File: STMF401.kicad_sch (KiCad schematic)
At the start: 26 parts, among them J6 Conn_01x04_Pin, U3 STM32F407VETx, Y1 X322525MQB4SI, Y2 SMD03215C2

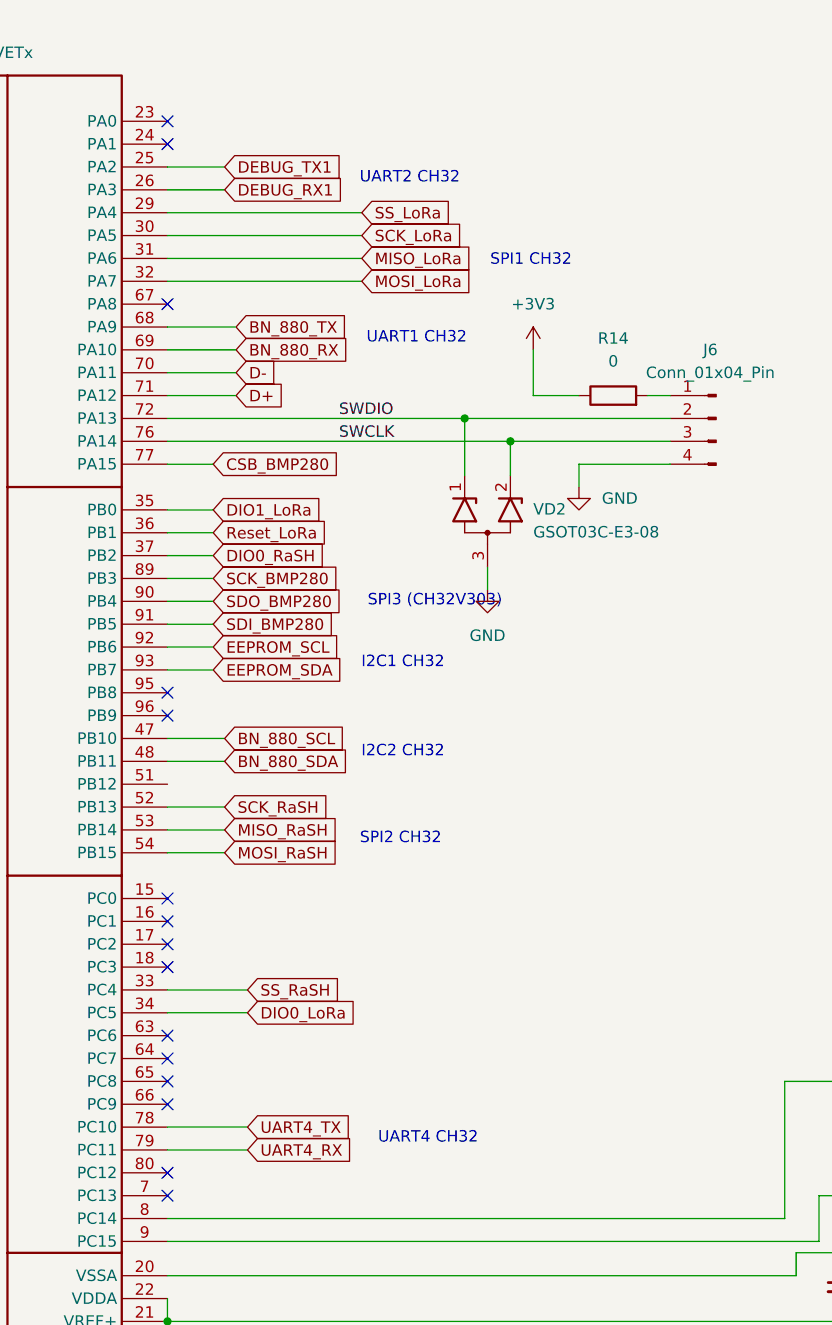
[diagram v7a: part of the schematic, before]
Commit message: feat: проведены сигнальные линии ко всем UART и USB
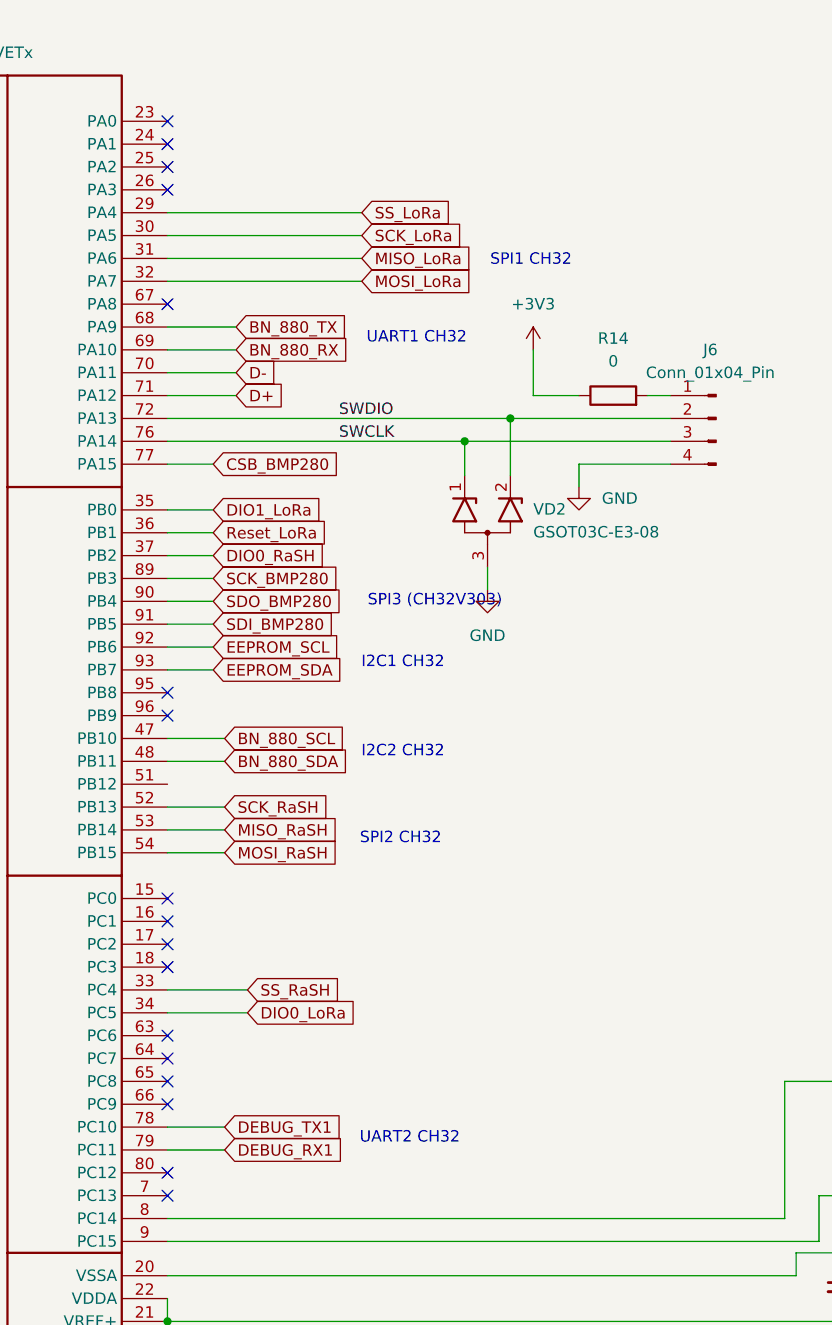
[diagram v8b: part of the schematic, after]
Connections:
- net UART4_RX is gone; now on net DEBUG_RX1: U3.79 (PC11)
- net UART4_TX is gone; now on net DEBUG_TX1: U3.78 (PC10)
- net DEBUG_RX1: no longer U3.26 (PA3)
- net DEBUG_TX1: no longer U3.25 (PA2)
- net SWCLK: now also VD2.1 (K1); no longer VD2.2 (K2)
- net SWDIO: now also VD2.2 (K2); no longer VD2.1 (K1)
- no-connect marks 18 -> 20
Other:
- note removed: "UART4 CH32"
